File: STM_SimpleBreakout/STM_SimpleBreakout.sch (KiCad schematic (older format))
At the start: 14 parts, among them J1 Screw_Terminal_01x05, J2 Screw_Terminal_01x16, J3 Screw_Terminal_01x16, U1 LD39015M33R, U2 STM32L031K6Tx

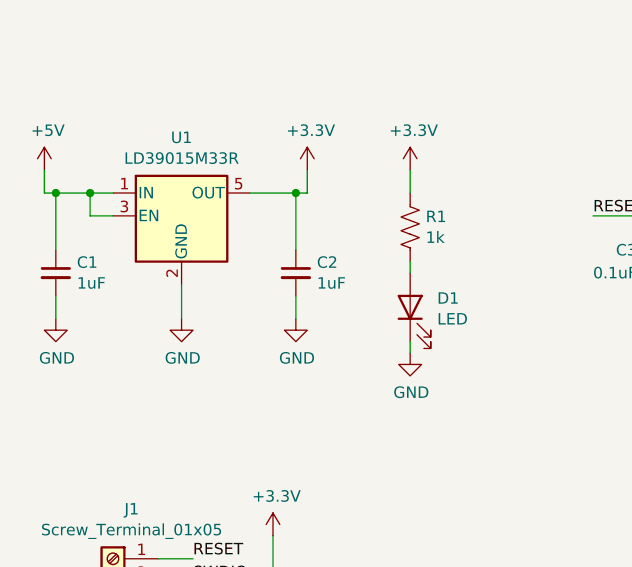
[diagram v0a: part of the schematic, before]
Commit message: Add in boost Converter and STM32 Breakout
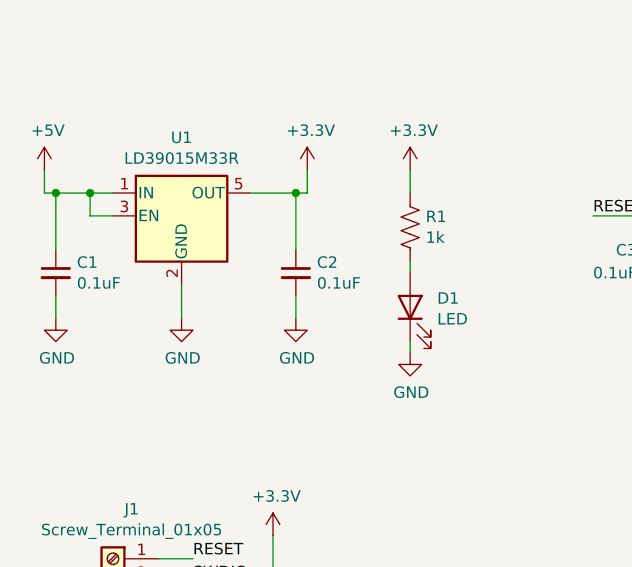
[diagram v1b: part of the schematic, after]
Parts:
- C1, C2: value 1uF -> 0.1uF
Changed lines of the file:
@@
 P 1400 3250
 F 0 "C1" H 1492 3296 50  0000 L CNN
-F 1 "1uF" H 1492 3205 50  0000 L CNN
+F 1 "0.1uF" H 1492 3205 50  0000 L CNN
 F 2 "Capacitor_SMD:C_0603_1608Metric_Pad1.08x0.95mm_HandSolder" H 1400 3250 50  0001 C CNN
 F 3 "~" H 1400 3250 50  0001 C CNN
@@
 P 2450 3250
 F 0 "C2" H 2542 3296 50  0000 L CNN
-F 1 "1uF" H 2542 3205 50  0000 L CNN
+F 1 "0.1uF" H 2542 3205 50  0000 L CNN
 F 2 "Capacitor_SMD:C_0603_1608Metric_Pad1.08x0.95mm_HandSolder" H 2450 3250 50  0001 C CNN
 F 3 "~" H 2450 3250 50  0001 C CNN
